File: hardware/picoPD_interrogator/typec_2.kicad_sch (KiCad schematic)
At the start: 26 parts, among them J2 USB_C_Receptacle_USB2.0_16P, Q1 rohm-RE1C002UN, Q2 rohm-RE1C002UN, Q4 rohm-RE1C002UN, Q5 rohm-RE1C002UN, U3 ST-LM393QT, U4 TI_SN74LVC1G3157-Q1, U5 TI_SN74LVC1G3157-Q1

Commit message: Working on schematic.
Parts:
- removed J2: USB_C_Receptacle_USB2.0_16P, Connector_USB:USB_C_Receptacle_GCT_USB4105-xx-A_16P_TopMnt_Horizontal, symbol Connector:USB_C_Receptacle_USB2.0_16P
- removed Q1, Q2, Q4, Q5: rohm-RE1C002UN, Package_TO_SOT_SMD:SOT-416, symbol picoPD_interrogator:rohm-RE1C002UN
- removed R10: 1K, Resistor_SMD:R_0201_0603Metric, symbol Device:R
- removed R11, R16: 200R, Resistor_SMD:R_0201_0603Metric, symbol Device:R
- removed R12, R17: 100R, Resistor_SMD:R_0201_0603Metric, symbol Device:R
- removed R14, R20: 0R, Resistor_SMD:R_0201_0603Metric, symbol Device:R
- removed R18, R19: 3.3K, Resistor_SMD:R_0201_0603Metric, symbol Device:R
- removed R22, R23: 33R, Resistor_SMD:R_0201_0603Metric, symbol Device:R
- removed R30, R31: 100K, Resistor_SMD:R_0201_0603Metric, symbol Device:R
- removed R4, R5: 35K, Resistor_SMD:R_0201_0603Metric, symbol Device:R
- removed R6, R7, R9: 5.1K, Resistor_SMD:R_0201_0603Metric, symbol Device:R
- removed U3: ST-LM393QT, picoPD_interrogator:DFN-8_2x2mm_P0.5mm_ST, symbol picoPD_interrogator:ST-LM393QT
- removed U4, U5: TI_SN74LVC1G3157-Q1, picoPD_interrogator:TI_sn741vc1g3157-q1, symbol picoPD_interrogator:TI_sn741vc1g3157-q1
- added J3: USB_C_Receptacle_USB2.0_16P, Connector_USB:USB_C_Receptacle_GCT_USB4105-xx-A_16P_TopMnt_Horizontal, symbol Connector:USB_C_Receptacle_USB2.0_16P
- added Q3, Q6, Q7, Q8: rohm-RE1C002UN, Package_TO_SOT_SMD:SOT-416, symbol picoPD_interrogator:rohm-RE1C002UN
- added R13, R40, R41: 5.1K, Resistor_SMD:R_0201_0603Metric, symbol Device:R
- added R32: 1K, Resistor_SMD:R_0201_0603Metric, symbol Device:R
- added R33, R42: 200R, Resistor_SMD:R_0201_0603Metric, symbol Device:R
- added R35, R43: 100R, Resistor_SMD:R_0201_0603Metric, symbol Device:R
- added R36, R8: 35K, Resistor_SMD:R_0201_0603Metric, symbol Device:R
- added R37, R46: 0R, Resistor_SMD:R_0201_0603Metric, symbol Device:R
- added R38, R47: 100K, Resistor_SMD:R_0201_0603Metric, symbol Device:R
- added R44, R45: 3.3K, Resistor_SMD:R_0201_0603Metric, symbol Device:R
- added R48, R49: 33R, Resistor_SMD:R_0201_0603Metric, symbol Device:R
- added U10, U9: TI_SN74LVC1G3157-Q1, picoPD_interrogator:TI_sn741vc1g3157-q1, symbol picoPD_interrogator:TI_sn741vc1g3157-q1
- added U8: ST-LM393QT, picoPD_interrogator:DFN-8_2x2mm_P0.5mm_ST, symbol picoPD_interrogator:ST-LM393QT
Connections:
- net 3V3: now also R13.2, R33.2, R36.2, R42.2, R44.1, R45.2, R48.2, R49.2, R8.2, U10.5 (VCC), U8.8 (V+), U9.5 (VCC)
- net BMC_VREF: now also R13.1, R32.2, U8.3 (+), U8.5 (+)
- net CC1_ADC: now also R38.1
- net CC1_CONN: now also J3.A5 (CC1), R36.1, R37.2, R41.2, U8.2 (-), U9.4 (A)
- net CC1_RX: now also R44.2, U8.1
- net CC1_TX: now also Q3.2 (S), Q6.3 (D), R37.1, R38.2
- net CC1_TX_H: now also Q3.1 (G)
- net CC1_TX_L: now also Q6.1 (G)
- net CC1_VCONN_EN: now also U9.6 (S)
- net CC2_ADC: now also R47.1
- net CC2_CONN: now also J3.B5 (CC2), R40.2, R46.1, R8.1, U10.4 (A), U8.6 (-)
- net CC2_RX: now also R45.1, U8.7
- net CC2_TX: now also Q7.2 (S), Q8.3 (D), R46.2, R47.2
- net CC2_TX_H: now also Q7.1 (G)
- net CC2_TX_L: now also Q8.1 (G)
- net CC2_VCONN_EN: now also U10.6 (S)
- net GND: now also J3.A1 (GND), J3.A12 (GND), J3.B1 (GND), J3.B12 (GND), J3.S1 (SHIELD), R32.1, R35.2, R40.1, R41.1, R43.2, U10.2 (GND), U8.4 (V-), U9.2 (GND)
- net SBU1: now also J3.A8 (SBU1)
- net SBU2: now also J3.B8 (SBU2)
- net USB_DM: now also J3.A7 (D-), J3.B7 (D-)
- net USB_DP: now also J3.A6 (D+), J3.B6 (D+)
- net VBUS: now also J3.A4 (VBUS), J3.A9 (VBUS), J3.B4 (VBUS), J3.B9 (VBUS)
- new net: Q8.2 (S), R43.1
- new net: Q3.3 (D), R33.1
- new net: Q7.3 (D), R42.1
- new net: Q6.2 (S), R35.1
- new net: R48.1, U9.1 (B2)
- new net: R49.1, U10.1 (B2)
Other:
- note added: "Interrogation Port 2 [USB-C receptacle]"
- note added: "Port 2 is configured with Rd resistors. (Default Role: UFP)"
- note removed: "Interrogation Port 1 [USB-C receptacle]"
- note removed: "Port 1 is configured with Rd resistors. (Default Role: UFP)"

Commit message: Updated schematic/BOM.
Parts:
- R13: DigiKey PN (none) -> P123051CT-N; Manufacturer (none) -> Panasonic Electronic Components; Manufacturer PN (none) -> ERJ-1GNF5101C
- R36, R8: DigiKey PN (none) -> P122955CT-ND; Manufacturer (none) -> Panasonic Industry; Manufacturer PN (none) -> ERJ-1GNF34R8C
- R38, R47: DigiKey PN RMCF0201ZT0R00CT-ND -> P122655CT-N; Manufacturer Stackpole Electronics Inc -> Panasonic Electronic Components; Manufacturer PN RMCF0201ZT0R00 -> ERJ-1GNF1003C

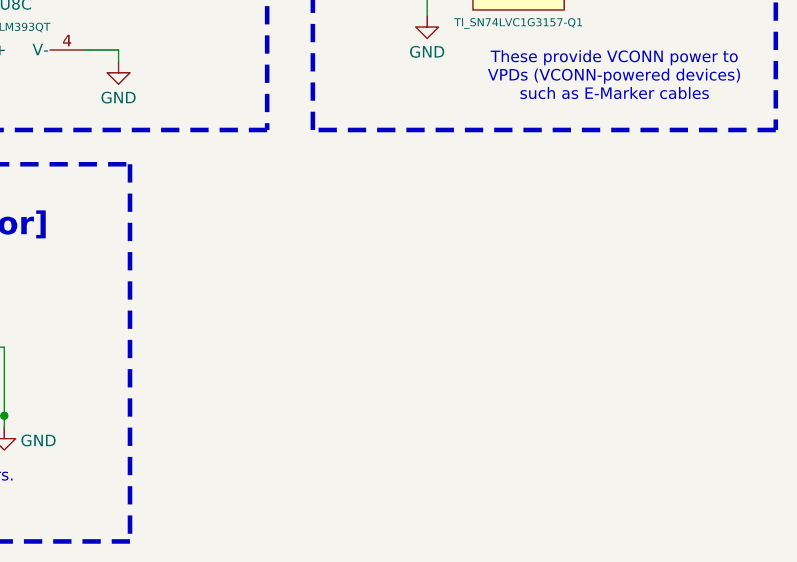
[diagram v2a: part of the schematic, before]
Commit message: Added 5v boost circuit, VBUS feedback to each port.
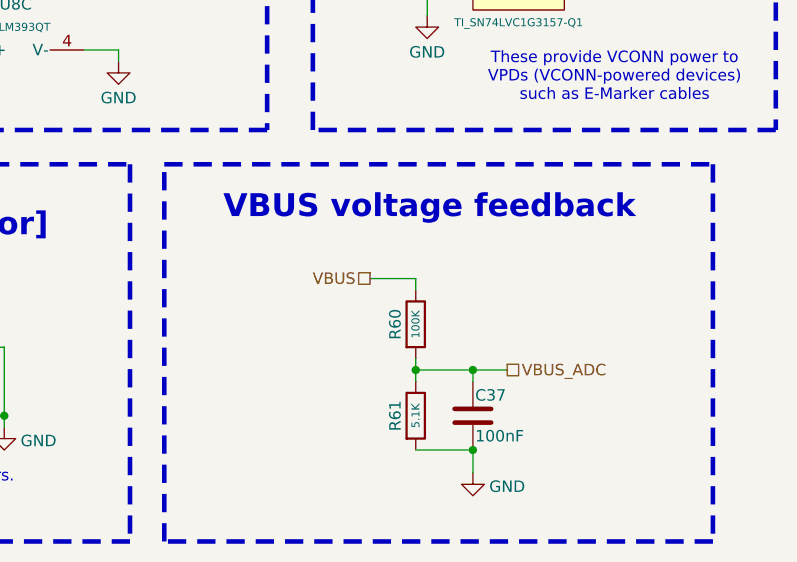
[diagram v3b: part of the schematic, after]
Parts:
- added C37: 100nF, Capacitor_SMD:C_0201_0603Metric, symbol Device:C
- added R60: 100K, Resistor_SMD:R_0201_0603Metric, symbol Device:R
- added R61: 5.1K, Resistor_SMD:R_0201_0603Metric, symbol Device:R
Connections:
- net GND: now also C37.2, R61.2
- net VBUS: now also R60.1
- new net VBUS_ADC: C37.1, R60.2, R61.1
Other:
- note added: "VBUS voltage feedback"

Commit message: Working on CYW43 stuff. Getting ready to test various PCB sizes.
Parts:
- R60: DigiKey PN (none) -> P122655CT-N; Manufacturer (none) -> Panasonic Electronic Components; Manufacturer PN (none) -> ERJ-1GNF1003C
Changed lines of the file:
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@@
 			)
 		)
-		(property "Description" ""
+		(property "Description" "RES SMD 100K OHM 1% 1/20W 0201"
 			(at 109.22 168.91 0)
 			(hide yes)
@@
 			)
 		)
-		(property "Manufacturer" ""
+		(property "Manufacturer" "Panasonic Electronic Components"
 			(at 109.22 168.91 0)
 			(hide yes)
@@
 			)
 		)
-		(property "DigiKey PN" ""
+		(property "DigiKey PN" "P122655CT-N"
 			(at 109.22 168.91 0)
 			(hide yes)
@@
 			)
 		)
-		(property "Manufacturer PN" ""
+		(property "Manufacturer PN" "ERJ-1GNF1003C"
 			(at 109.22 168.91 0)
 			(hide yes)

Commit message: Working on basic layout.
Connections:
- net GND: no longer J3.S1 (SHIELD)
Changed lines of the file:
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@@
 	)
 	(junction
-		(at 115.57 73.66)
-		(diameter 0)
-		(color 0 0 0 0)
-	)
-	(junction
 		(at 115.57 173.99)
 		(diameter 0)
@@
 	(wire
 		(pts
-			(xy 107.95 73.66) (xy 115.57 73.66)
-		)
-		(stroke
-			(width 0)
-			(type default)
-		)
-	)
-	(wire
-		(pts
 			(xy 130.81 53.34) (xy 132.08 53.34)
 		)
@@
 		(pin "A9"
 		)
-		(pin "S1"
-		)
 		(pin "A1"
